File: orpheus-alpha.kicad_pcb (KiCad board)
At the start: 2 copper layers, 98 x 59.3 mm, 61 parts, among them J1 Signal in, J2 AC in, J3 Signal out, J4 uC, J5 CONN_01X03, U1 OPA2134, U2 PGA2311, U3 LM317_3PinPackage, U4 LM337_SOT223, U5 LM7805_TO220

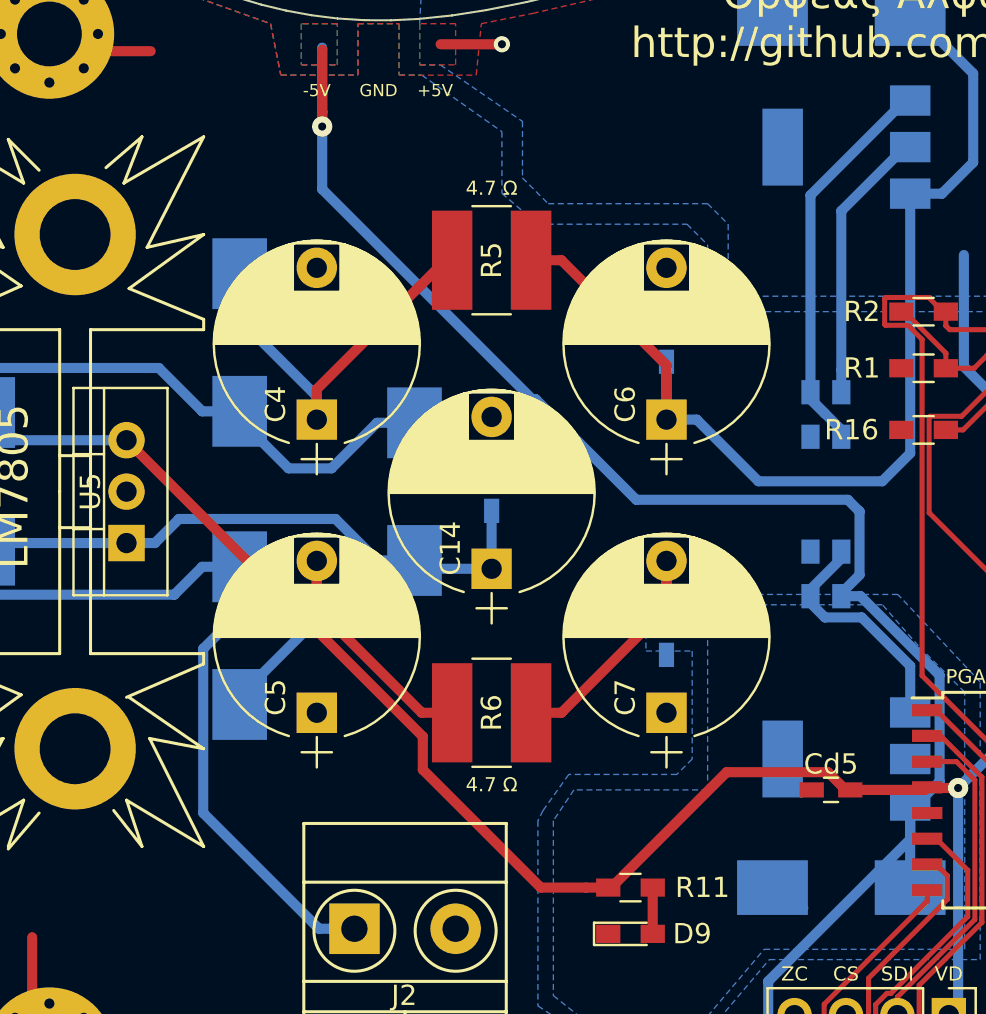
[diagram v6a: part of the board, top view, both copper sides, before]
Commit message: Changed footprint of PSU capacitors
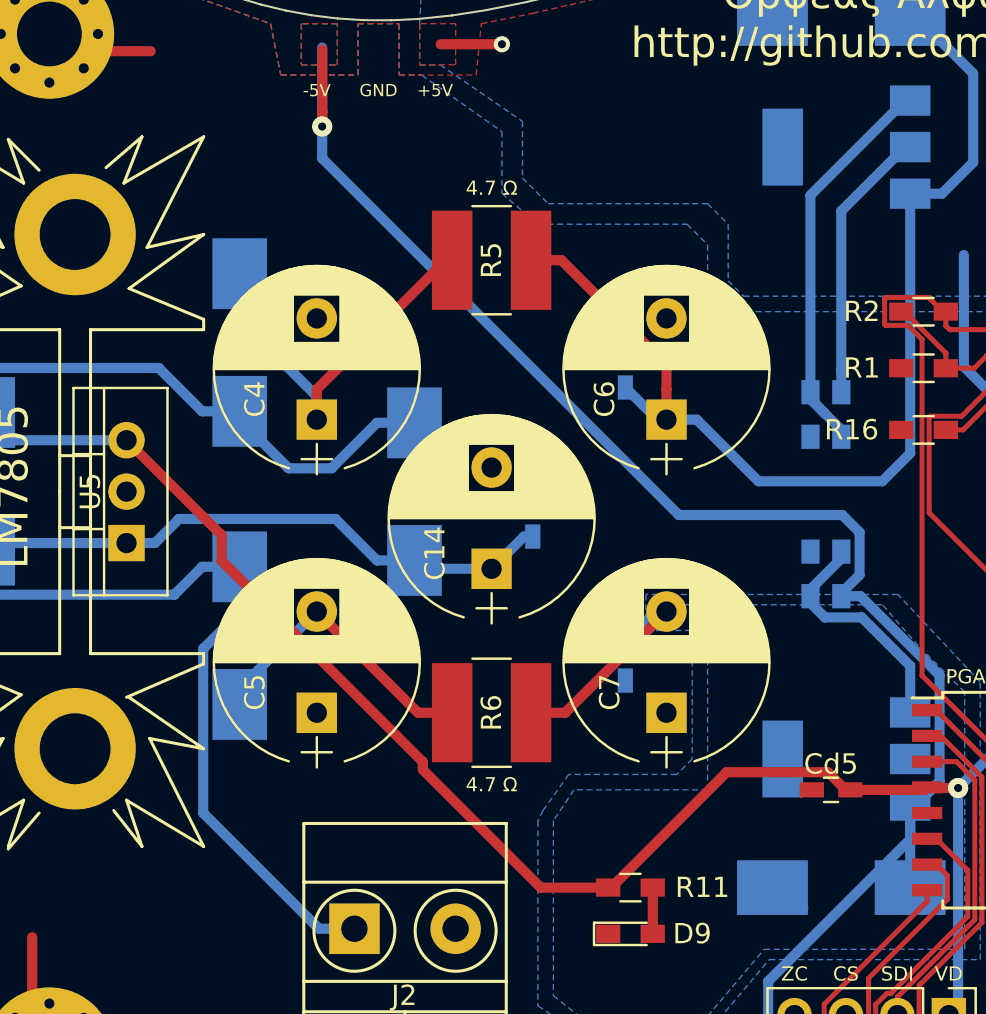
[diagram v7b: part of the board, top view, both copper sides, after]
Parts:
- C14, C4, C5, C6, C7: footprint Capacitors_THT:CP_Radial_D10.0mm_P7.50mm -> Capacitors_THT:CP_Radial_D10.0mm_P5.00mm
- moved C15 2.40 mm to (110.7, 105.9)
- moved C8 2.40 mm to (115.3, 98.6)
- moved C9 2.40 mm to (115.3, 113.0)
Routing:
- net Net-(C5-Pad2): track 19.8 -> 15.3 mm
- net Net-(C7-Pad2): track 14.3 -> 11.8 mm
- net V-: track 247.9 -> 246.4 mm
